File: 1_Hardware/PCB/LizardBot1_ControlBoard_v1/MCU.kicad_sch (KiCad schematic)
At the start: 29 parts, among them J301 2.54mm (M), J302 2.54mm (M), J303 USB_C_Receptacle_USB2.0_16P, Q301 UMH3N, SW301 SW_Push, SW302 SW_Push, SW303 SW_SPST, U301 ESP32-WROOM-32E, U302 USBLC6-2P6, U303 CP2102N-Axx-xQFN24

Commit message: Added Peripherals schematic
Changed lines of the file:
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@@
 	)
 	(hierarchical_label "MCU_BUZZER"
-		(shape input)
+		(shape output)
 		(at 46.99 177.8 180)
 		(fields_autoplaced yes)
@@
 	)
 	(hierarchical_label "MCU_TXD0"
-		(shape input)
+		(shape output)
 		(at 124.46 46.99 0)
 		(fields_autoplaced yes)
@@
 	)
 	(hierarchical_label "MCU_NEOPIXEL"
-		(shape input)
+		(shape output)
 		(at 124.46 67.31 0)
 		(fields_autoplaced yes)
@@
 	)
 	(hierarchical_label "MCU_FAN_PWM"
-		(shape input)
+		(shape output)
 		(at 124.46 57.15 0)
 		(fields_autoplaced yes)
@@
 	)
 	(hierarchical_label "MCU_SDA"
-		(shape input)
+		(shape bidirectional)
 		(at 124.46 82.55 0)
 		(fields_autoplaced yes)
@@
 	)
 	(hierarchical_label "MCU_SCL"
-		(shape input)
+		(shape bidirectional)
 		(at 124.46 85.09 0)
 		(fields_autoplaced yes)
@@
 	)
 	(hierarchical_label "MCU_BUZZER"
-		(shape input)
+		(shape output)
 		(at 124.46 64.77 0)
 		(fields_autoplaced yes)
@@
 	)
 	(hierarchical_label "MCU_TXD0"
-		(shape input)
+		(shape output)
 		(at 173.99 101.6 180)
 		(fields_autoplaced yes)
@@
 	)
 	(hierarchical_label "MCU_FAN_PWM"
-		(shape input)
+		(shape output)
 		(at 114.3 162.56 0)
 		(fields_autoplaced yes)

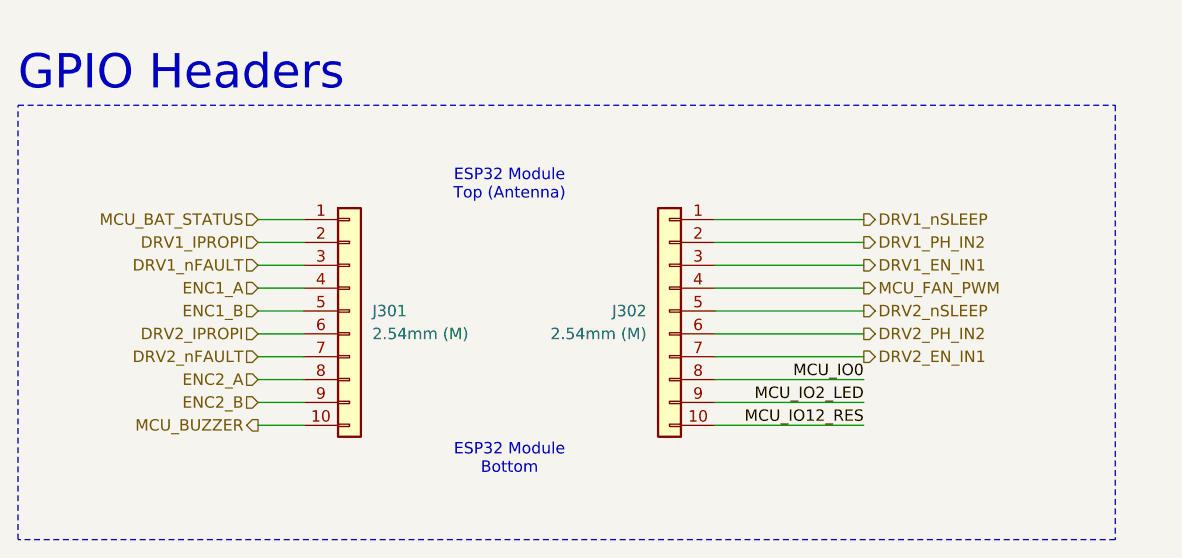
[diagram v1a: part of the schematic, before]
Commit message: Added Communication_Interfaces schematic
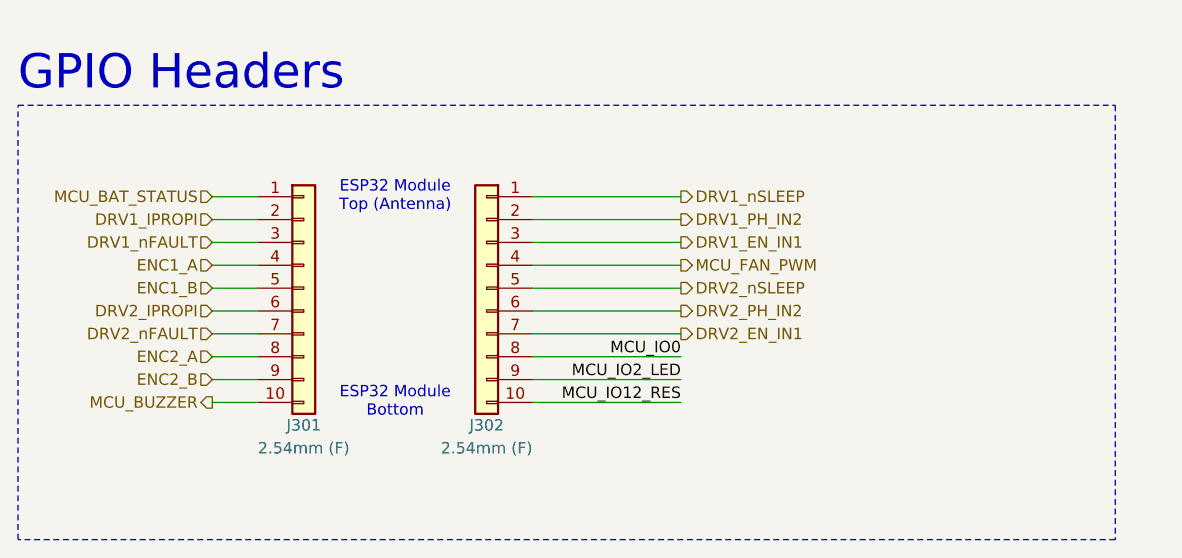
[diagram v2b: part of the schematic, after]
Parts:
- J301, J302: value 2.54mm (M) -> 2.54mm (F)
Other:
- moved on the sheet: J301, J302
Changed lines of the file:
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@@
 	(wire
 		(pts
-			(xy 97.79 154.94) (xy 114.3 154.94)
+			(xy 77.47 152.4) (xy 93.98 152.4)
 		)
 		(stroke
@@
 	(wire
 		(pts
-			(xy 97.79 175.26) (xy 114.3 175.26)
+			(xy 77.47 172.72) (xy 93.98 172.72)
 		)
 		(stroke
@@
 	(wire
 		(pts
-			(xy 52.07 170.18) (xy 46.99 170.18)
+			(xy 46.99 167.64) (xy 41.91 167.64)
 		)
 		(stroke
@@
 	(wire
 		(pts
-			(xy 97.79 177.8) (xy 114.3 177.8)
+			(xy 77.47 175.26) (xy 93.98 175.26)
 		)
 		(stroke
@@
 	(wire
 		(pts
-			(xy 52.07 167.64) (xy 46.99 167.64)
+			(xy 46.99 165.1) (xy 41.91 165.1)
 		)
 		(stroke
@@
 	(wire
 		(pts
-			(xy 52.07 172.72) (xy 46.99 172.72)
+			(xy 46.99 170.18) (xy 41.91 170.18)
 		)
 		(stroke
@@
 	(wire
 		(pts
-			(xy 52.07 160.02) (xy 46.99 160.02)
+			(xy 46.99 157.48) (xy 41.91 157.48)
 		)
 		(stroke
@@
 	(wire
 		(pts
-			(xy 52.07 162.56) (xy 46.99 162.56)
+			(xy 46.99 160.02) (xy 41.91 160.02)
 		)
 		(stroke
@@
 	(wire
 		(pts
-			(xy 97.79 160.02) (xy 114.3 160.02)
+			(xy 77.47 157.48) (xy 93.98 157.48)
 		)
 		(stroke
@@
 	(wire
 		(pts
-			(xy 52.07 177.8) (xy 46.99 177.8)
+			(xy 46.99 175.26) (xy 41.91 175.26)
 		)
 		(stroke
@@
 	(wire
 		(pts
-			(xy 52.07 157.48) (xy 46.99 157.48)
+			(xy 46.99 154.94) (xy 41.91 154.94)
 		)
 		(stroke
@@
 	(wire
 		(pts
-			(xy 97.79 172.72) (xy 114.3 172.72)
+			(xy 77.47 170.18) (xy 93.98 170.18)
 		)
 		(stroke
@@
 	(wire
 		(pts
-			(xy 97.79 162.56) (xy 114.3 162.56)
+			(xy 77.47 160.02) (xy 93.98 160.02)
 		)
 		(stroke
@@
 	(wire
 		(pts
-			(xy 97.79 165.1) (xy 114.3 165.1)
+			(xy 77.47 162.56) (xy 93.98 162.56)
 		)
 		(stroke
@@
 	(wire
 		(pts
-			(xy 97.79 170.18) (xy 114.3 170.18)
+			(xy 77.47 167.64) (xy 93.98 167.64)
 		)
 		(stroke
@@
 	(wire
 		(pts
-			(xy 52.07 154.94) (xy 46.99 154.94)
+			(xy 46.99 152.4) (xy 41.91 152.4)
 		)
 		(stroke
@@
 	(wire
 		(pts
-			(xy 97.79 167.64) (xy 114.3 167.64)
+			(xy 77.47 165.1) (xy 93.98 165.1)
 		)
 		(stroke
@@
 	(wire
 		(pts
-			(xy 97.79 157.48) (xy 114.3 157.48)
+			(xy 77.47 154.94) (xy 93.98 154.94)
 		)
 		(stroke
@@
 	(wire
 		(pts
-			(xy 52.07 165.1) (xy 46.99 165.1)
+			(xy 46.99 162.56) (xy 41.91 162.56)
 		)
 		(stroke
@@
 	(wire
 		(pts
-			(xy 52.07 175.26) (xy 46.99 175.26)
+			(xy 46.99 172.72) (xy 41.91 172.72)
 		)
 		(stroke
@@
 	(text "ESP32 Module\nTop (Antenna)"
 		(exclude_from_sim no)
-		(at 74.93 151.13 0)
+		(at 62.23 152.4 0)
 		(effects
 			(font
@@
 	(text "ESP32 Module\nBottom"
 		(exclude_from_sim no)
-		(at 74.93 181.61 0)
+		(at 62.23 175.26 0)
 		(effects
 			(font
@@
 	)
 	(label "MCU_IO12_RES"
-		(at 114.3 177.8 180)
+		(at 93.98 175.26 180)
 		(fields_autoplaced yes)
 		(effects
@@
 	)
 	(label "MCU_IO0"
-		(at 114.3 172.72 180)
+		(at 93.98 170.18 180)
 		(fields_autoplaced yes)
 		(effects
@@
 	)
 	(label "MCU_IO2_LED"
-		(at 114.3 175.26 180)
+		(at 93.98 172.72 180)
 		(fields_autoplaced yes)
 		(effects
@@
 	(hierarchical_label "ENC2_B"
 		(shape input)
-		(at 46.99 175.26 180)
+		(at 41.91 172.72 180)
 		(fields_autoplaced yes)
 		(effects
@@
 	(hierarchical_label "MCU_BUZZER"
 		(shape output)
-		(at 46.99 177.8 180)
+		(at 41.91 175.26 180)
 		(fields_autoplaced yes)
 		(effects
@@
 	(hierarchical_label "DRV1_nSLEEP"
 		(shape output)
-		(at 114.3 154.94 0)
+		(at 93.98 152.4 0)
 		(fields_autoplaced yes)
 		(effects
@@
 	(hierarchical_label "MCU_BAT_STATUS"
 		(shape input)
-		(at 46.99 154.94 180)
+		(at 41.91 152.4 180)
 		(fields_autoplaced yes)
 		(effects
@@
 	(hierarchical_label "ENC2_A"
 		(shape input)
-		(at 46.99 172.72 180)
+		(at 41.91 170.18 180)
 		(fields_autoplaced yes)
 		(effects
@@
 	(hierarchical_label "DRV2_PH_IN2"
 		(shape output)
-		(at 114.3 167.64 0)
+		(at 93.98 165.1 0)
 		(fields_autoplaced yes)
 		(effects
@@
 	(hierarchical_label "DRV2_nFAULT"
 		(shape input)
-		(at 46.99 170.18 180)
+		(at 41.91 167.64 180)
 		(fields_autoplaced yes)
 		(effects
@@
 	(hierarchical_label "DRV1_EN_IN1"
 		(shape output)
-		(at 114.3 160.02 0)
+		(at 93.98 157.48 0)
 		(fields_autoplaced yes)
 		(effects
@@
 	(hierarchical_label "DRV2_IPROPI"
 		(shape input)
-		(at 46.99 167.64 180)
+		(at 41.91 165.1 180)
 		(fields_autoplaced yes)
 		(effects
@@
 	(hierarchical_label "DRV2_nSLEEP"
 		(shape output)
-		(at 114.3 165.1 0)
+		(at 93.98 162.56 0)
 		(fields_autoplaced yes)
 		(effects
@@
 	(hierarchical_label "DRV2_EN_IN1"
 		(shape output)
-		(at 114.3 170.18 0)
+		(at 93.98 167.64 0)
 		(fields_autoplaced yes)
 		(effects
@@
 	(hierarchical_label "DRV1_nFAULT"
 		(shape input)
-		(at 46.99 160.02 180)
+		(at 41.91 157.48 180)
 		(fields_autoplaced yes)
 		(effects
@@
 	(hierarchical_label "ENC1_A"
 		(shape input)
-		(at 46.99 162.56 180)
+		(at 41.91 160.02 180)
 		(fields_autoplaced yes)
 		(effects
@@
 	(hierarchical_label "ENC1_B"
 		(shape input)
-		(at 46.99 165.1 180)
+		(at 41.91 162.56 180)
 		(fields_autoplaced yes)
 		(effects
@@
 	(hierarchical_label "DRV1_PH_IN2"
 		(shape output)
-		(at 114.3 157.48 0)
+		(at 93.98 154.94 0)
 		(fields_autoplaced yes)
 		(effects
@@
 	(hierarchical_label "DRV1_IPROPI"
 		(shape input)
-		(at 46.99 157.48 180)
+		(at 41.91 154.94 180)
 		(fields_autoplaced yes)
 		(effects
@@
 	(hierarchical_label "MCU_FAN_PWM"
 		(shape output)
-		(at 114.3 162.56 0)
+		(at 93.98 160.02 0)
 		(fields_autoplaced yes)
 		(effects
@@
 	(symbol
 		(lib_id "Connector_Generic:Conn_01x10")
-		(at 92.71 165.1 0)
+		(at 72.39 162.56 0)
 		(mirror y)
 		(unit 1)
@@
 		(dnp no)
 		(property "Reference" "J302"
-			(at 90.17 165.0999 0)
+			(at 72.39 177.8 0)
 			(effects
 				(font
 					(size 1.27 1.27)
 				)
-				(justify left)
 			)
 		)
-		(property "Value" "2.54mm (M)"
-			(at 90.17 167.6399 0)
+		(property "Value" "2.54mm (F)"
+			(at 72.39 180.34 0)
 			(effects
 				(font
 					(size 1.27 1.27)
 				)
-				(justify left)
 			)
 		)
 		(property "Footprint" ""
-			(at 92.71 165.1 0)
+			(at 72.39 162.56 0)
 			(effects
 				(font
@@
 		)
 		(property "Datasheet" "~"
-			(at 92.71 165.1 0)
+			(at 72.39 162.56 0)
 			(effects
 				(font
@@
 		)
 		(property "Description" "Generic connector, single row, 01x10, script generated (kicad-library-utils/schlib/autogen/connector/)"
-			(at 92.71 165.1 0)
+			(at 72.39 162.56 0)
 			(effects
 				(font
@@
 	(symbol
 		(lib_id "Connector_Generic:Conn_01x10")
-		(at 57.15 165.1 0)
+		(at 52.07 162.56 0)
 		(unit 1)
 		(exclude_from_sim no)
@@
 		(on_board yes)
 		(dnp no)
-		(fields_autoplaced yes)
 		(property "Reference" "J301"
-			(at 59.69 165.0999 0)
+			(at 52.07 177.8 0)
 			(effects
 				(font
 					(size 1.27 1.27)
 				)
-				(justify left)
 			)
 		)
-		(property "Value" "2.54mm (M)"
-			(at 59.69 167.6399 0)
+		(property "Value" "2.54mm (F)"
+			(at 52.07 180.34 0)
 			(effects
 				(font
 					(size 1.27 1.27)
 				)
-				(justify left)
 			)
 		)
 		(property "Footprint" ""
-			(at 57.15 165.1 0)
+			(at 52.07 162.56 0)
 			(effects
 				(font
@@
 		)
 		(property "Datasheet" "~"
-			(at 57.15 165.1 0)
+			(at 52.07 162.56 0)
 			(effects
 				(font
@@
 		)
 		(property "Description" "Generic connector, single row, 01x10, script generated (kicad-library-utils/schlib/autogen/connector/)"
-			(at 57.15 165.1 0)
+			(at 52.07 162.56 0)
 			(effects
 				(font

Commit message: PCB schematics revision
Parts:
- added F301: 500mA, symbol Device:Polyfuse_Small
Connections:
- net VBUS: now also F301.2; no longer J303.A4 (VBUS), J303.A9 (VBUS), J303.B4 (VBUS), J303.B9 (VBUS)
- new net USBC_VBUS: F301.1, J303.A4 (VBUS), J303.A9 (VBUS), J303.B4 (VBUS), J303.B9 (VBUS)
- no-connect marks 3 -> 13
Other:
- moved on the sheet: J301, J302, R303, R304, R305, R306, R310, U302

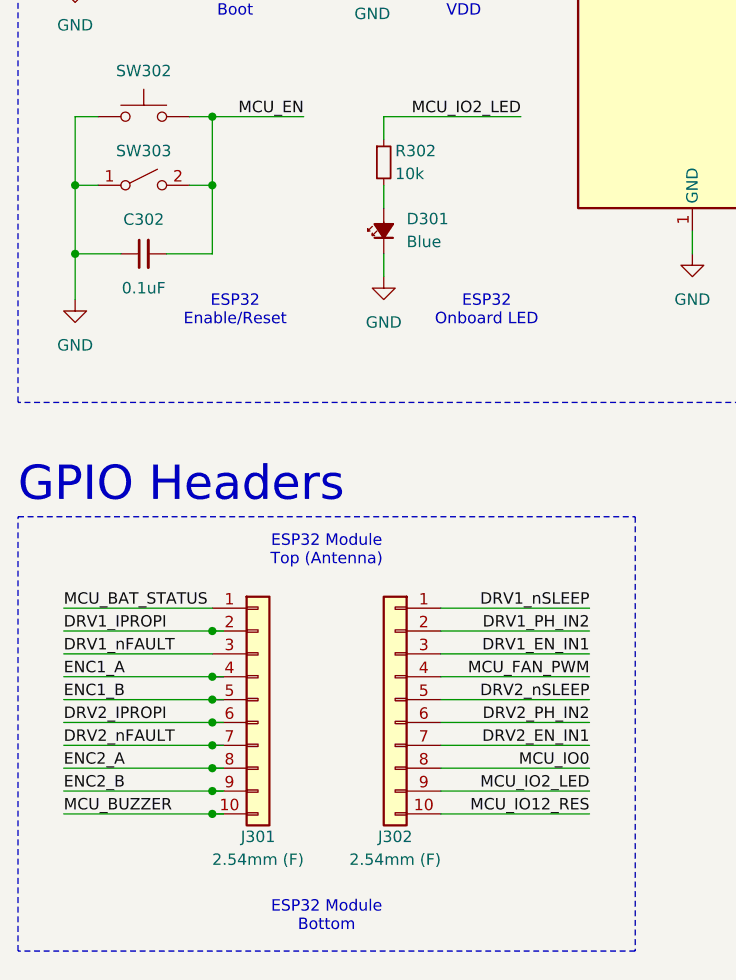
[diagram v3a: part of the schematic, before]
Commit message: Updated schematics. Assigned footprints. Added BOM to /4_Docs.
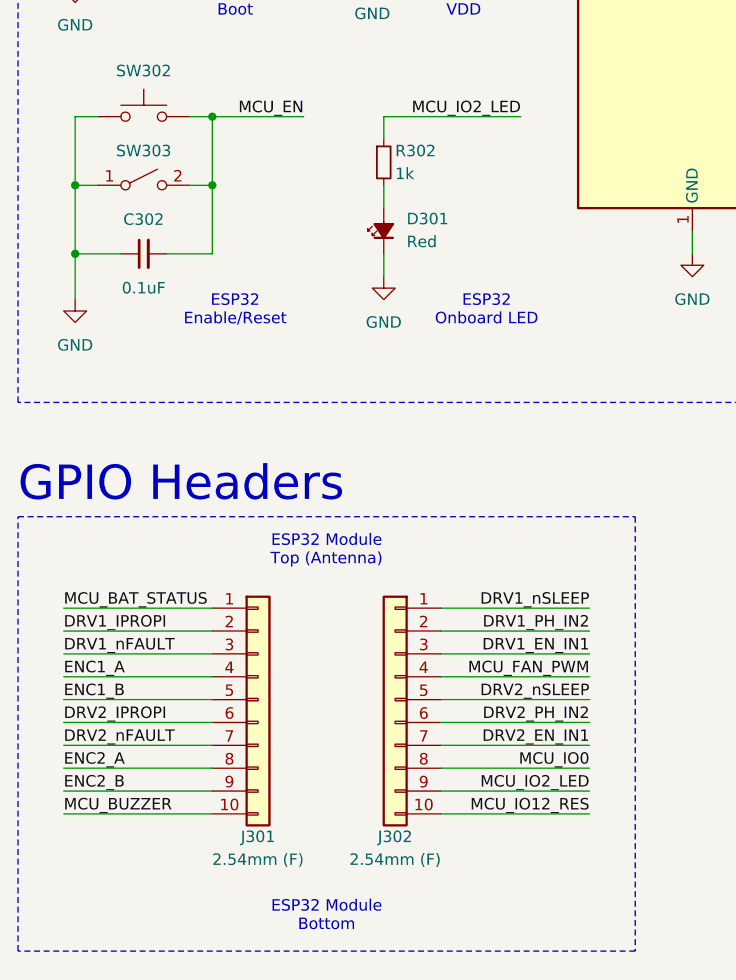
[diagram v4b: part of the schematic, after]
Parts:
- C301, C302, C303: footprint (none) -> Capacitor_SMD:C_0603_1608Metric_Pad1.08x0.95mm_HandSolder
- C304, C305, C306, C307, C308: footprint (none) -> Capacitor_SMD:C_0805_2012Metric_Pad1.18x1.45mm_HandSolder
- D301: value Blue -> Red; footprint (none) -> LED_SMD:LED_1206_3216Metric_Pad1.42x1.75mm_HandSolder
- F301: footprint (none) -> Fuse:Fuse_1206_3216Metric_Pad1.42x1.75mm_HandSolder
- J301, J302: footprint (none) -> Connector_PinHeader_2.54mm:PinHeader_1x10_P2.54mm_Vertical
- J303: footprint (none) -> Connector_USB:USB_C_Receptacle_GCT_USB4085
- R301, R303, R304, R305, R306, R307, R308, R309, R310: footprint (none) -> Resistor_SMD:R_0603_1608Metric_Pad0.98x0.95mm_HandSolder
- R302: value 10k -> 1k; footprint (none) -> Resistor_SMD:R_0603_1608Metric_Pad0.98x0.95mm_HandSolder
- SW301, SW302: footprint (none) -> Button_Switch_SMD:SW_SPST_TL3342
- SW303: footprint (none) -> Button_Switch_THT:SW_Slide_SPDT_Straight_CK_OS102011MS2Q
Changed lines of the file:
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@@
 	)
 	(junction
-		(at 41.91 162.56)
-		(diameter 0)
-		(color 0 0 0 0)
-	)
-	(junction
-		(at 41.91 160.02)
-		(diameter 0)
-		(color 0 0 0 0)
-	)
-	(junction
 		(at 205.74 120.65)
 		(diameter 0)
@@
 	)
 	(junction
-		(at 41.91 175.26)
-		(diameter 0)
-		(color 0 0 0 0)
-	)
-	(junction
 		(at 215.9 128.27)
 		(diameter 0)
@@
 	)
 	(junction
-		(at 41.91 172.72)
-		(diameter 0)
-		(color 0 0 0 0)
-	)
-	(junction
 		(at 39.37 69.85)
 		(diameter 0)
@@
 	)
 	(junction
-		(at 41.91 167.64)
-		(diameter 0)
-		(color 0 0 0 0)
-	)
-	(junction
-		(at 41.91 170.18)
-		(diameter 0)
-		(color 0 0 0 0)
-	)
-	(junction
 		(at 41.91 97.79)
 		(diameter 0)
@@
 	)
 	(junction
-		(at 41.91 165.1)
-		(diameter 0)
-		(color 0 0 0 0)
-	)
-	(junction
 		(at 243.84 35.56)
 		(diameter 0)
@@
 	)
 	(junction
-		(at 41.91 154.94)
-		(diameter 0)
-		(color 0 0 0 0)
-	)
-	(junction
 		(at 26.67 113.03)
 		(diameter 0)
@@
 	(wire
 		(pts
-			(xy 43.18 170.18) (xy 41.91 170.18)
-		)
-		(stroke
-			(width 0)
-			(type default)
-		)
-	)
-	(wire
-		(pts
 			(xy 59.69 72.39) (xy 69.85 72.39)
 		)
@@
 	(wire
 		(pts
-			(xy 43.18 154.94) (xy 41.91 154.94)
-		)
-		(stroke
-			(width 0)
-			(type default)
-		)
-	)
-	(wire
-		(pts
 			(xy 67.31 175.26) (xy 83.82 175.26)
 		)
@@
 	(wire
 		(pts
-			(xy 43.18 167.64) (xy 41.91 167.64)
-		)
-		(stroke
-			(width 0)
-			(type default)
-		)
-	)
-	(wire
-		(pts
 			(xy 58.42 52.07) (xy 80.01 52.07)
 		)
@@
 	(wire
 		(pts
-			(xy 43.18 172.72) (xy 41.91 172.72)
-		)
-		(stroke
-			(width 0)
-			(type default)
-		)
-	)
-	(wire
-		(pts
 			(xy 110.49 46.99) (xy 129.54 46.99)
 		)
@@
 	(wire
 		(pts
-			(xy 43.18 175.26) (xy 41.91 175.26)
-		)
-		(stroke
-			(width 0)
-			(type default)
-		)
-	)
-	(wire
-		(pts
-			(xy 43.18 160.02) (xy 41.91 160.02)
-		)
-		(stroke
-			(width 0)
-			(type default)
-		)
-	)
-	(wire
-		(pts
 			(xy 41.91 97.79) (xy 52.07 97.79)
 		)
@@
 	(wire
 		(pts
-			(xy 43.18 165.1) (xy 41.91 165.1)
-		)
-		(stroke
-			(width 0)
-			(type default)
-		)
-	)
-	(wire
-		(pts
 			(xy 67.31 170.18) (xy 83.82 170.18)
 		)
@@
 	(wire
 		(pts
-			(xy 43.18 162.56) (xy 41.91 162.56)
-		)
-		(stroke
-			(width 0)
-			(type default)
-		)
-	)
-	(wire
-		(pts
 			(xy 218.44 60.96) (xy 233.68 60.96)
 		)
@@
 			)
 		)
-		(property "Footprint" ""
+		(property "Footprint" "Resistor_SMD:R_0603_1608Metric_Pad0.98x0.95mm_HandSolder"
 			(at 172.72 93.98 0)
 			(effects
@@
 			)
 		)
-		(property "Footprint" ""
+		(property "Footprint" "Capacitor_SMD:C_0805_2012Metric_Pad1.18x1.45mm_HandSolder"
 			(at 59.69 76.2 0)
 			(effects
@@
 			)
 		)
-		(property "Footprint" ""
+		(property "Footprint" "Connector_PinHeader_2.54mm:PinHeader_1x10_P2.54mm_Vertical"
 			(at 62.23 162.56 0)
 			(effects
@@
 			)
 		)
-		(property "Footprint" ""
+		(property "Footprint" "Resistor_SMD:R_0603_1608Metric_Pad0.98x0.95mm_HandSolder"
 			(at 215.9 133.35 0)
 			(effects
@@
 			)
 		)
-		(property "Footprint" ""
+		(property "Footprint" "Resistor_SMD:R_0603_1608Metric_Pad0.98x0.95mm_HandSolder"
 			(at 210.82 128.27 0)
 			(effects
@@
 			)
 		)
-		(property "Value" "Blue"
+		(property "Value" "Red"
 			(at 63.5 111.6964 90)
 			(effects
@@
 			)
 		)
-		(property "Footprint" ""
+		(property "Footprint" "LED_SMD:LED_1206_3216Metric_Pad1.42x1.75mm_HandSolder"
 			(at 60.96 110.49 90)
 			(effects
@@
 			)
 		)
-		(property "Footprint" ""
+		(property "Footprint" "Resistor_SMD:R_0603_1608Metric_Pad0.98x0.95mm_HandSolder"
 			(at 220.98 38.1 0)
 			(effects
@@
 			)
 		)
-		(property "Footprint" ""
+		(property "Footprint" "Capacitor_SMD:C_0805_2012Metric_Pad1.18x1.45mm_HandSolder"
 			(at 160.02 121.92 0)
 			(effects
@@
 			)
 		)
-		(property "Footprint" ""
+		(property "Footprint" "Resistor_SMD:R_0603_1608Metric_Pad0.98x0.95mm_HandSolder"
 			(at 172.72 101.6 0)
 			(effects
@@
 			)
 		)
-		(property "Footprint" ""
+		(property "Footprint" "Fuse:Fuse_1206_3216Metric_Pad1.42x1.75mm_HandSolder"
 			(at 209.55 41.91 0)
 			(effects
@@
 			)
 		)
-		(property "Footprint" ""
+		(property "Footprint" "Capacitor_SMD:C_0805_2012Metric_Pad1.18x1.45mm_HandSolder"
 			(at 189.23 121.92 0)
 			(effects
@@
 			)
 		)
-		(property "Footprint" ""
+		(property "Footprint" "Resistor_SMD:R_0603_1608Metric_Pad0.98x0.95mm_HandSolder"
 			(at 196.85 78.74 0)
 			(effects
@@
 			)
 		)
-		(property "Footprint" ""
+		(property "Footprint" "Capacitor_SMD:C_0805_2012Metric_Pad1.18x1.45mm_HandSolder"
 			(at 170.18 121.92 0)
 			(effects
@@
 			)
 		)
-		(property "Value" "10k"
+		(property "Value" "1k"
 			(at 62.23 104.14 0)
 			(effects
@@
 			)
 		)
-		(property "Footprint" ""
+		(property "Footprint" "Resistor_SMD:R_0603_1608Metric_Pad0.98x0.95mm_HandSolder"
 			(at 60.96 102.87 0)
 			(effects
@@
 			)
 		)
-		(property "Footprint" ""
+		(property "Footprint" "Connector_USB:USB_C_Receptacle_GCT_USB4085"
 			(at 173.99 58.42 0)
 			(effects
@@
 			)
 		)
-		(property "Footprint" ""
+		(property "Footprint" "Resistor_SMD:R_0603_1608Metric_Pad0.98x0.95mm_HandSolder"
 			(at 205.74 78.74 0)
 			(effects
@@
 			)
 		)
-		(property "Footprint" ""
+		(property "Footprint" "Capacitor_SMD:C_0603_1608Metric_Pad1.08x0.95mm_HandSolder"
 			(at 34.29 113.03 0)
 			(effects
@@
 			)
 		)
-		(property "Footprint" ""
+		(property "Footprint" "Button_Switch_THT:SW_Slide_SPDT_Straight_CK_OS102011MS2Q"
 			(at 34.29 105.41 0)
 			(effects
@@
 			)
 		)
-		(property "Footprint" ""
+		(property "Footprint" "Connector_PinHeader_2.54mm:PinHeader_1x10_P2.54mm_Vertical"
 			(at 46.99 162.56 0)
 			(effects
@@
 			)
 		)
-		(property "Footprint" ""
+		(property "Footprint" "Resistor_SMD:R_0603_1608Metric_Pad0.98x0.95mm_HandSolder"
 			(at 210.82 120.65 0)
 			(effects
@@
 			)
 		)
-		(property "Footprint" ""
+		(property "Footprint" "Capacitor_SMD:C_0603_1608Metric_Pad1.08x0.95mm_HandSolder"
 			(at 33.02 76.2 0)
 			(effects
@@
 			)
 		)
-		(property "Footprint" ""
+		(property "Footprint" "Capacitor_SMD:C_0805_2012Metric_Pad1.18x1.45mm_HandSolder"
 			(at 69.85 76.2 0)
 			(effects
@@
 			)
 		)
-		(property "Footprint" ""
+		(property "Footprint" "Resistor_SMD:R_0603_1608Metric_Pad0.98x0.95mm_HandSolder"
 			(at 50.8 40.64 0)
 			(effects
@@
 			)
 		)
-		(property "Footprint" ""
+		(property "Footprint" "Button_Switch_SMD:SW_SPST_TL3342"
 			(at 33.02 64.77 0)
 			(effects
@@
 			)
 		)
-		(property "Footprint" ""
+		(property "Footprint" "Button_Switch_SMD:SW_SPST_TL3342"
 			(at 34.29 92.71 0)
 			(effects
@@
 			)
 		)
-		(property "Footprint" ""
+		(property "Footprint" "Capacitor_SMD:C_0603_1608Metric_Pad1.08x0.95mm_HandSolder"
 			(at 44.45 44.45 0)
 			(effects
